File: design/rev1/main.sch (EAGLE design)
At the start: 43 parts, among them J1 ICSP-HEADER1X6-0.1-ICSP-PADS, J2 HEADER-141X14-0.1-PADS, SW1 JS102000SAQN, SW2 JS102000SAQN, SW3 B3U-3000P, U1 PIC18F2XK20, U2 LIS3DSH, U3 APDS-9008

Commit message: [CNG] - more schematic and layout progress on rev1
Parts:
- added C7: 0.1uF, matt:CAPACITOR0603
- C2: device matt:CAPACITOR0805 -> matt:CAPACITOR0603
- D1, D10, D2, D3, D4, D5, D6, D7, D8, D9: value LED0402 -> LED0603; device matt:LED0402 -> matt:LED0603
- J2: value HEADER-141X14-0.1-PADS -> HEADER-141X14-0.05-PADS; device matt:HEADER-141X14-0.1-PADS -> matt:HEADER-141X14-0.05-PADS
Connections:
- removed net N$1: B1.P$+, B2.P$+, SW1.3
- new net V_BATT: B1.P$+, B2.P$+, C1.1, L1.1, REG1.VIN, SW1.3
- net +3V3: now also J1.VDD
- net ACCEL_INT1: now also J2.4; no longer J2.11
- net ACCEL_INT2: now also J2.5; no longer J2.12
- net GND: now also C7.2, J2.1, SW1.2; no longer J2.14
- net LIGHT_VSENSE: now also J2.6; no longer J2.10
- net PIC_CS: now also J2.13; no longer J2.4
- net PIC_EXT_FUNC: now also J2.9; no longer J2.13
- net PIC_RX: now also J2.3; no longer J2.2
- net PIC_SCK: now also J2.10; no longer J2.5
- net PIC_SDI: now also J2.12; no longer J2.7
- net PIC_SDO: now also J2.11; no longer J2.6
- net PIC_TX: now also J2.2; no longer J2.3
- net PROG_EN: now also J2.7; no longer J2.9
- net V_SW: now also C7.1, J2.14; no longer C1.1, J1.VDD, J2.1, L1.1, REG1.VIN
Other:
- note added: "Boost Converter"
- note added: "Power Switch/Batteries"
- note removed: "Regulator"
- note removed: "Switch/Battery Holders"
- moved on the sheet: B1, B2, C2, J2, SW1

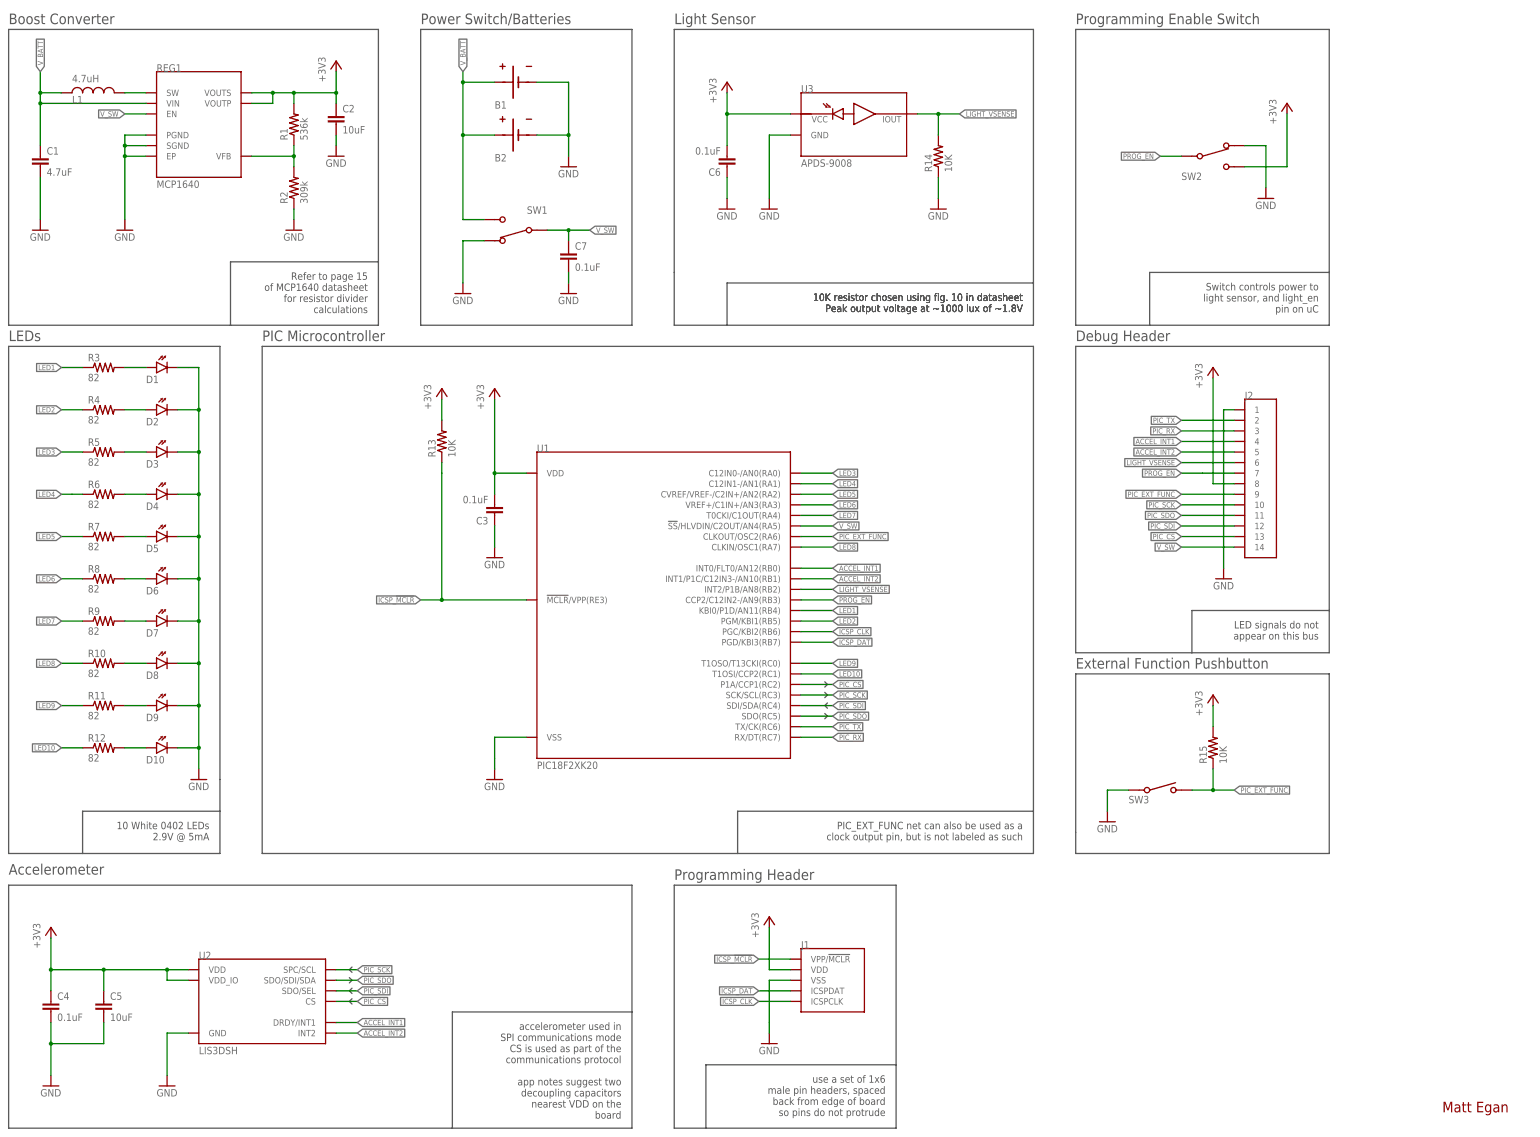
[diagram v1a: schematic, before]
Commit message: [CNG] - finished most of the new electrical changes for rev1 (see planning.txt), starting layout
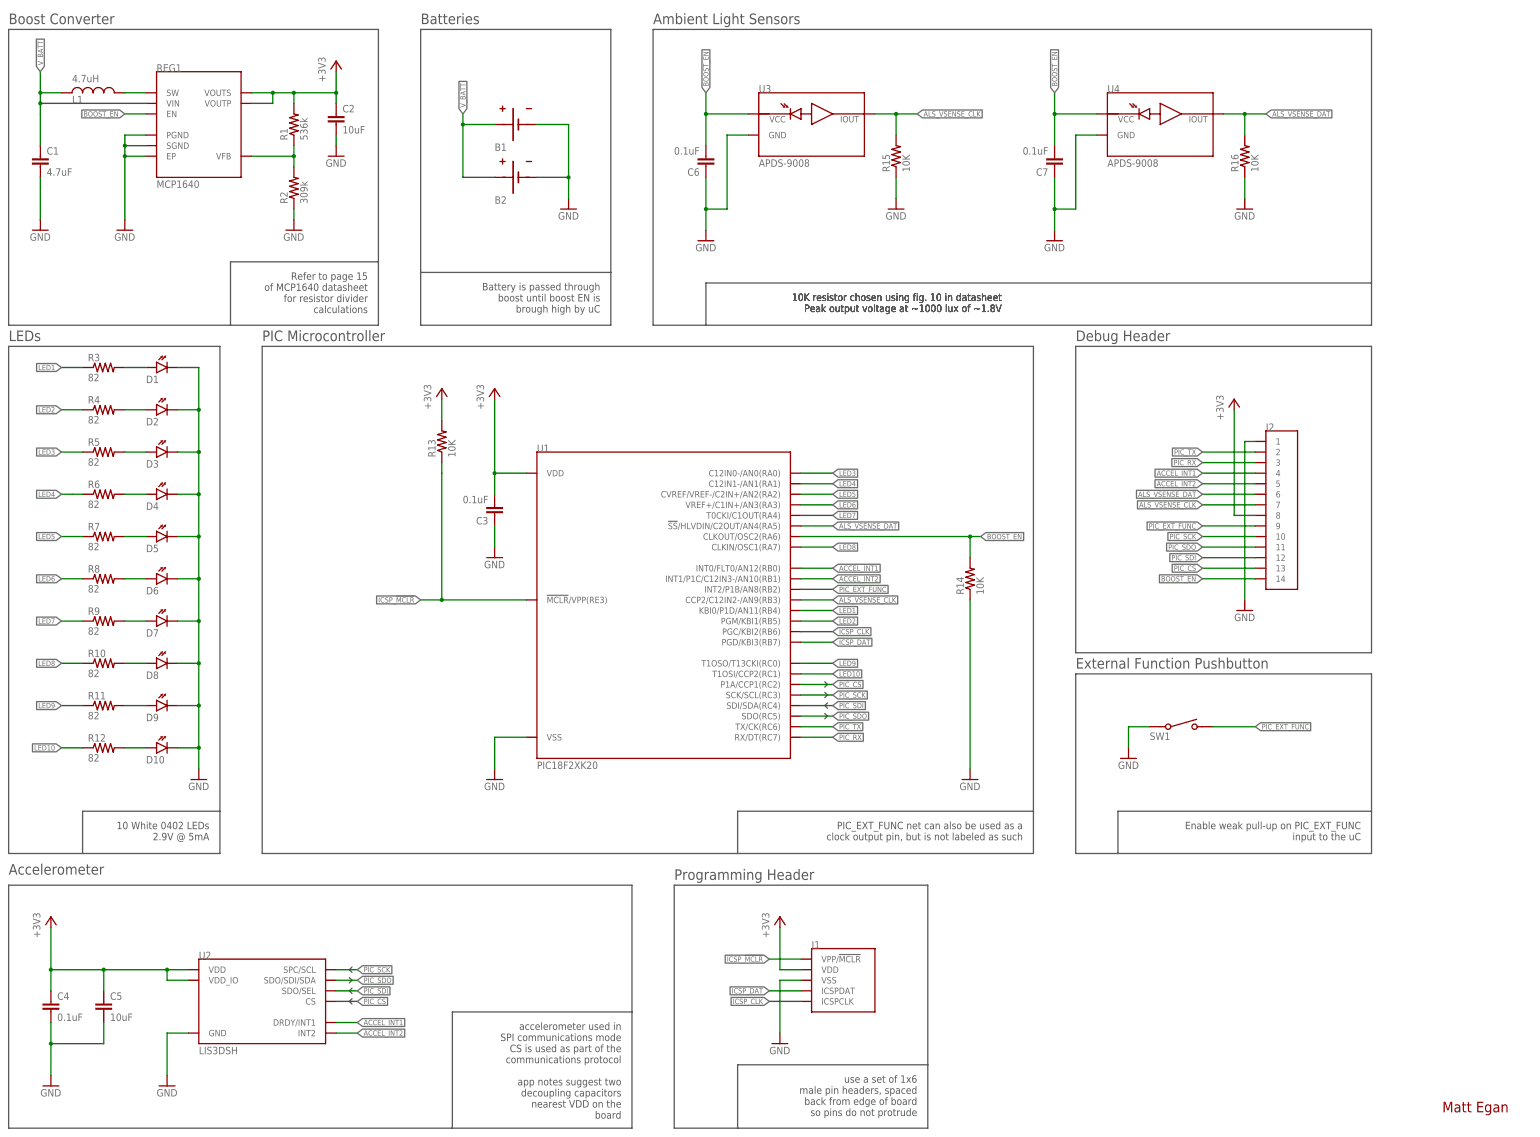
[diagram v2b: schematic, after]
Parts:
- removed SW2: JS102000SAQN, matt:JS102000SAQN
- removed SW3: B3U-3000P, matt:B3U-3000P
- added R16: 10K, matt:RESISTOR0603
- added U4: APDS-9008, matt:APDS-9008
- C7: device matt:CAPACITOR0603 -> matt:CAPACITOR0805
- SW1: value JS102000SAQN -> B3U-3000P; device matt:JS102000SAQN -> matt:B3U-3000P
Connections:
- removed net LIGHT_VSENSE: J2.6, R14.2, U1.INT2/P1B/AN8(RB2), U3.P$IOUT
- removed net PROG_EN: J2.7, SW2.1, U1.CCP2/C12IN2-/AN9(RB3)
- removed net V_SW: C7.1, J2.14, REG1.EN, SW1.1, U1.!SS!/HLVDIN/C2OUT/AN4(RA5)
- new net ALS_VSENSE_CLK: J2.7, R15.2, U1.CCP2/C12IN2-/AN9(RB3), U3.P$IOUT
- new net ALS_VSENSE_DAT: J2.6, R16.2, U1.!SS!/HLVDIN/C2OUT/AN4(RA5), U4.P$IOUT
- new net BOOST_EN: C6.2, C7.2, J2.14, R14.2, REG1.EN, U1.CLKOUT/OSC2(RA6), U3.P$VCC, U4.P$VCC
- net +3V3: no longer C6.2, R15.2, SW2.3, U3.P$VCC
- net GND: now also C7.1, R15.1, R16.1, SW1.1, U4.GND; no longer C7.2, SW1.2, SW2.2, SW3.1
- net PIC_EXT_FUNC: now also SW1.3, U1.INT2/P1B/AN8(RB2); no longer R15.1, SW3.3, U1.CLKOUT/OSC2(RA6)
- net V_BATT: no longer SW1.3
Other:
- note added: "Ambient Light Sensors"
- note added: "Batteries"
- note added: "Battery is passed through boost until boost EN is brough high by uC"
- note added: "Enable weak pull-up on PIC_EXT_FUNC input to the uC"
- note removed: "LED signals do not appear on this bus"
- note removed: "Light Sensor"
- note removed: "Power Switch/Batteries"
- note removed: "Programming Enable Switch"
- note removed: "Switch controls power to light sensor, and light_en pin on uC"
- moved on the sheet: B1, B2, C6, C7, J1, J2, R14, R15, U3
